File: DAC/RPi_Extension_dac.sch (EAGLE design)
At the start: 41 parts, among them U1 AD5360BSTZ, U2 ADR423ARZ

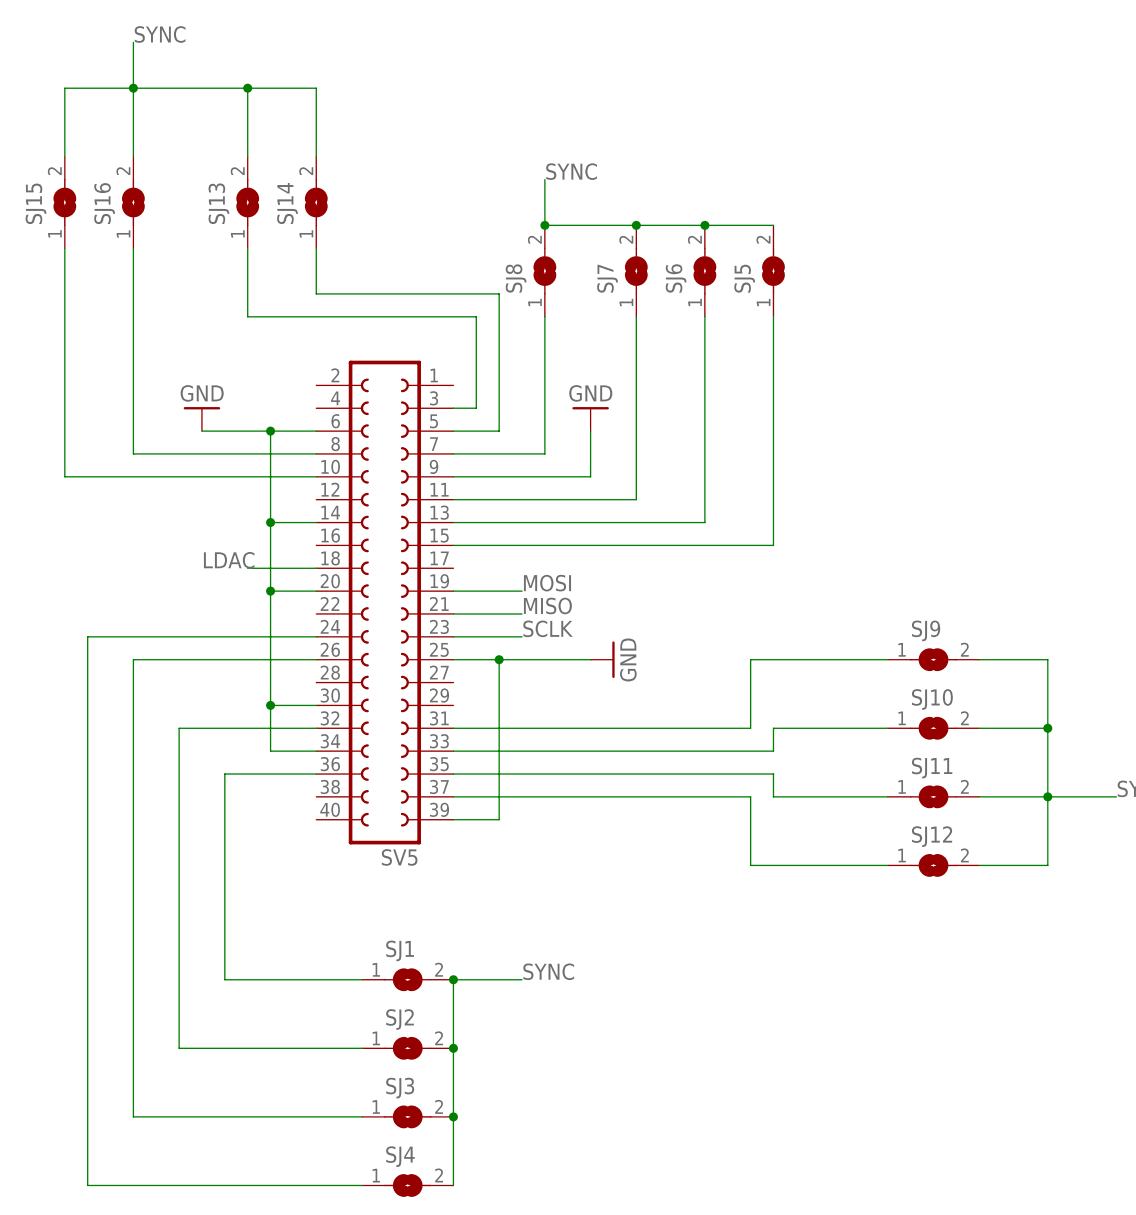
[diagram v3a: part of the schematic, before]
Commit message: cleaned up silklayer of dac board
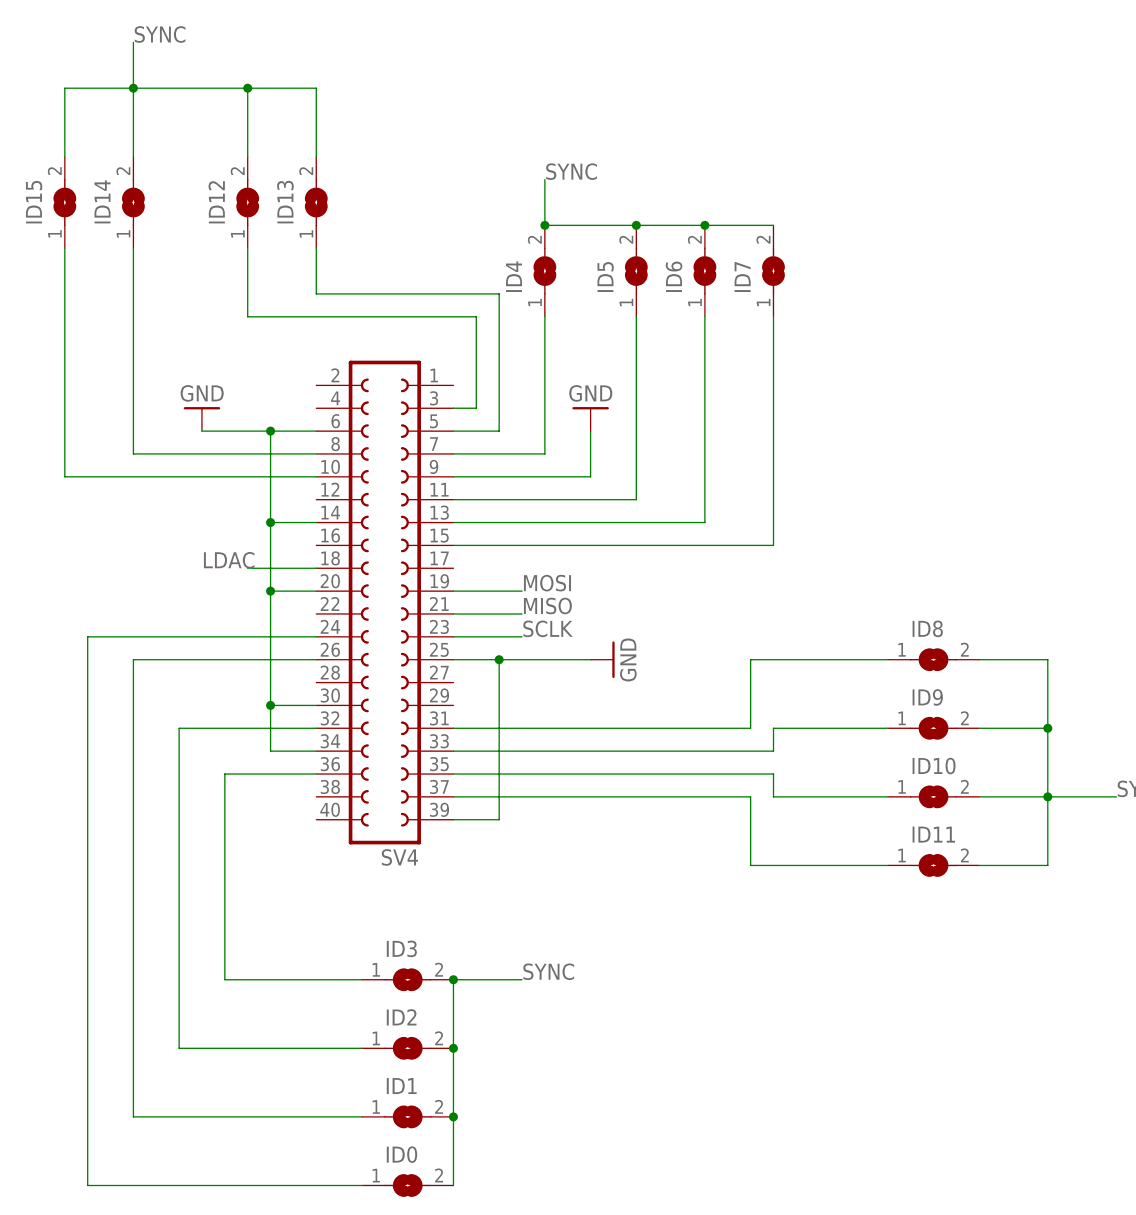
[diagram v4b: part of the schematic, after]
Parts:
- renumbered SJ1 to ID3, SJ10 to ID9, SJ11 to ID10, SJ12 to ID11, SJ13 to ID12, SJ14 to ID13, SJ15 to ID15, SJ16 to ID14, SJ2 to ID2, SJ3 to ID1, SJ4 to ID0, SJ5 to ID7, SJ6 to ID6, SJ7 to ID5, SJ8 to ID4, SJ9 to ID8, SV5 to SV4

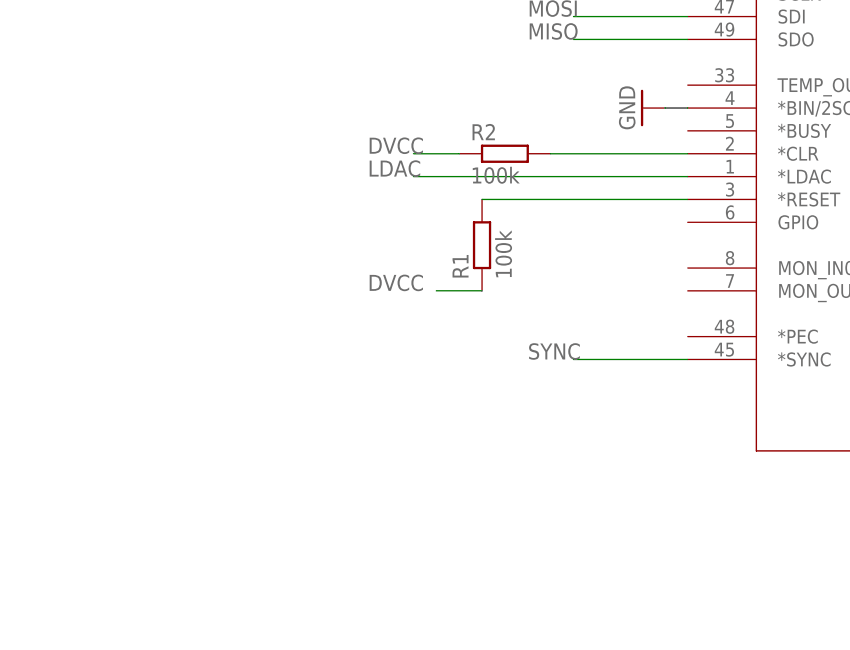
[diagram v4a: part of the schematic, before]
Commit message: updated content before making repository public
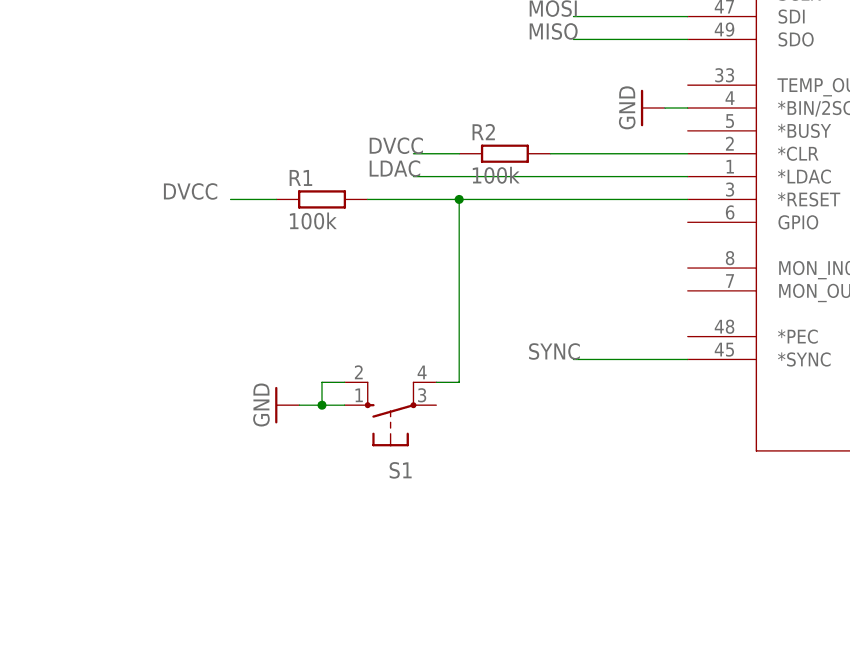
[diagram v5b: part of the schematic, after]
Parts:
- added S1: (no value), switch-omron:10-XX
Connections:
- net GND: now also S1.S, S1.S1
- net N$18: now also S1.P1
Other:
- moved on the sheet: R1
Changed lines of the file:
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@@
 <?xml version="1.0" encoding="utf-8"?>
 <!DOCTYPE eagle SYSTEM "eagle.dtd">
-<eagle version="7.6.0">
+<eagle version="8.1.0">
 <drawing>
 <settings>
@@
 <part name="ID15" library="jumper" deviceset="SJ" device=""/>
 <part name="ID14" library="jumper" deviceset="SJ" device=""/>
+<part name="S1" library="switch-omron" deviceset="10-XX" device=""/>
+<part name="GND13" library="supply1" deviceset="GND" device=""/>
 </parts>
 <sheets>
@@
 <instance part="GND11" gate="1" x="-106.68" y="68.58" rot="R180"/>
 <instance part="GND12" gate="1" x="-63.5" y="68.58" rot="R180"/>
-<instance part="R1" gate="G$1" x="68.58" y="63.5" rot="R90"/>
+<instance part="R1" gate="G$1" x="50.8" y="68.58"/>
 <instance part="R2" gate="G$1" x="71.12" y="73.66"/>
 <instance part="ID8" gate="1" x="-25.4" y="40.64"/>
@@
 <instance part="ID15" gate="1" x="-121.92" y="91.44" rot="R90"/>
 <instance part="ID14" gate="1" x="-114.3" y="91.44" rot="R90"/>
+<instance part="S1" gate="1" x="58.42" y="45.72" rot="R90"/>
+<instance part="GND13" gate="1" x="45.72" y="45.72" rot="R270"/>
 </instances>
 <busses>
@@
 <junction x="215.9" y="40.64"/>
 </segment>
+<segment>
+<pinref part="S1" gate="1" pin="S"/>
+<pinref part="GND13" gate="1" pin="GND"/>
+<wire x1="53.34" y1="45.72" x2="50.8" y2="45.72" width="0.1524" layer="91"/>
+<pinref part="S1" gate="1" pin="S1"/>
+<wire x1="50.8" y1="45.72" x2="48.26" y2="45.72" width="0.1524" layer="91"/>
+<wire x1="53.34" y1="48.26" x2="50.8" y2="48.26" width="0.1524" layer="91"/>
+<wire x1="50.8" y1="48.26" x2="50.8" y2="45.72" width="0.1524" layer="91"/>
+<junction x="50.8" y="45.72"/>
+</segment>
 </net>
 <net name="DVCC" class="0">
@@
 <segment>
 <pinref part="R1" gate="G$1" pin="1"/>
-<wire x1="68.58" y1="58.42" x2="63.5" y2="58.42" width="0.1524" layer="91"/>
-<label x="55.88" y="58.42" size="1.778" layer="95"/>
+<wire x1="45.72" y1="68.58" x2="40.64" y2="68.58" width="0.1524" layer="91"/>
+<label x="33.02" y="68.58" size="1.778" layer="95"/>
 </segment>
 </net>
@@
 <pinref part="U1" gate="A" pin="*RESET"/>
 <pinref part="R1" gate="G$1" pin="2"/>
-<wire x1="91.44" y1="68.58" x2="68.58" y2="68.58" width="0.1524" layer="91"/>
-</segment>
-</net>
+<wire x1="91.44" y1="68.58" x2="66.04" y2="68.58" width="0.1524" layer="91"/>
+<pinref part="S1" gate="1" pin="P1"/>
+<wire x1="66.04" y1="68.58" x2="55.88" y2="68.58" width="0.1524" layer="91"/>
+<wire x1="63.5" y1="48.26" x2="66.04" y2="48.26" width="0.1524" layer="91"/>
+<wire x1="66.04" y1="48.26" x2="66.04" y2="68.58" width="0.1524" layer="91"/>
+<junction x="66.04" y="68.58"/>
+</segment>
+</net>

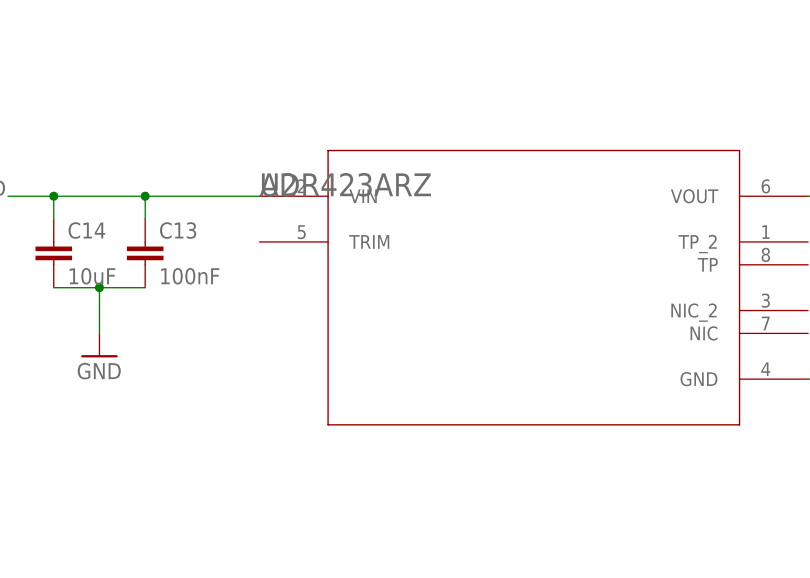
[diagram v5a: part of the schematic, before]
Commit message: updated reference voltage on dac board
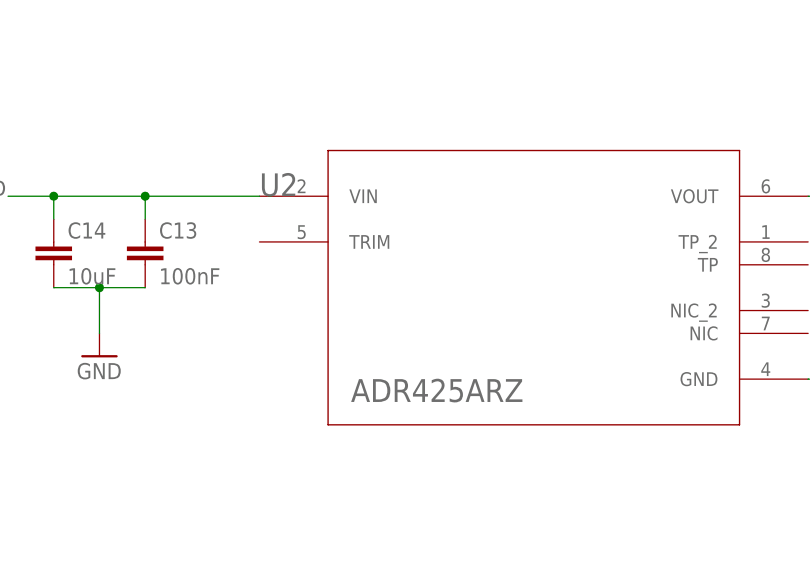
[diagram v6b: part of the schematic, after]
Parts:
- U2: value ADR423ARZ -> ADR425ARZ
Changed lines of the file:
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@@
 <?xml version="1.0" encoding="utf-8"?>
 <!DOCTYPE eagle SYSTEM "eagle.dtd">
-<eagle version="8.1.0">
+<eagle version="8.4.3">
 <drawing>
 <settings>
 <setting alwaysvectorfont="no"/>
+<setting keepoldvectorfont="yes"/>
 <setting verticaltext="up"/>
 </settings>
@@
 <part name="ID0" library="jumper" deviceset="SJ" device=""/>
 <part name="GND6" library="supply1" deviceset="GND" device=""/>
-<part name="U2" library="ADR423ARZ" deviceset="ADR423ARZ" device=""/>
+<part name="U2" library="ADR423ARZ" deviceset="ADR423ARZ" device="" value="ADR425ARZ"/>
 <part name="GND7" library="supply1" deviceset="GND" device=""/>
 <part name="C13" library="rcl" deviceset="C-EU" device="C0603" value="100nF"/>
@@
 <instance part="ID0" gate="1" x="-83.82" y="-17.78"/>
 <instance part="GND6" gate="1" x="86.36" y="78.74" rot="R270"/>
-<instance part="U2" gate="A" x="248.92" y="116.84"/>
+<instance part="U2" gate="A" x="248.92" y="116.84" smashed="yes">
+<attribute name="NAME" x="248.92" y="116.84" size="2.54" layer="95" ratio="10" rot="SR0"/>
+<attribute name="VALUE" x="259.08" y="93.98" size="2.54" layer="96" ratio="10" rot="SR0"/>
+</instance>
 <instance part="GND7" gate="1" x="231.14" y="99.06"/>
 <instance part="C13" gate="G$1" x="236.22" y="111.76"/>
